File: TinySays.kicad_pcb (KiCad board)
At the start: 2 copper layers, 50 x 50 mm, 30 parts, among them IC1 ATTINY85-S, P2 USB_OTG, P3 CONN_01X02, SW1 Switch_SPDT_x2, U1 MCP73831

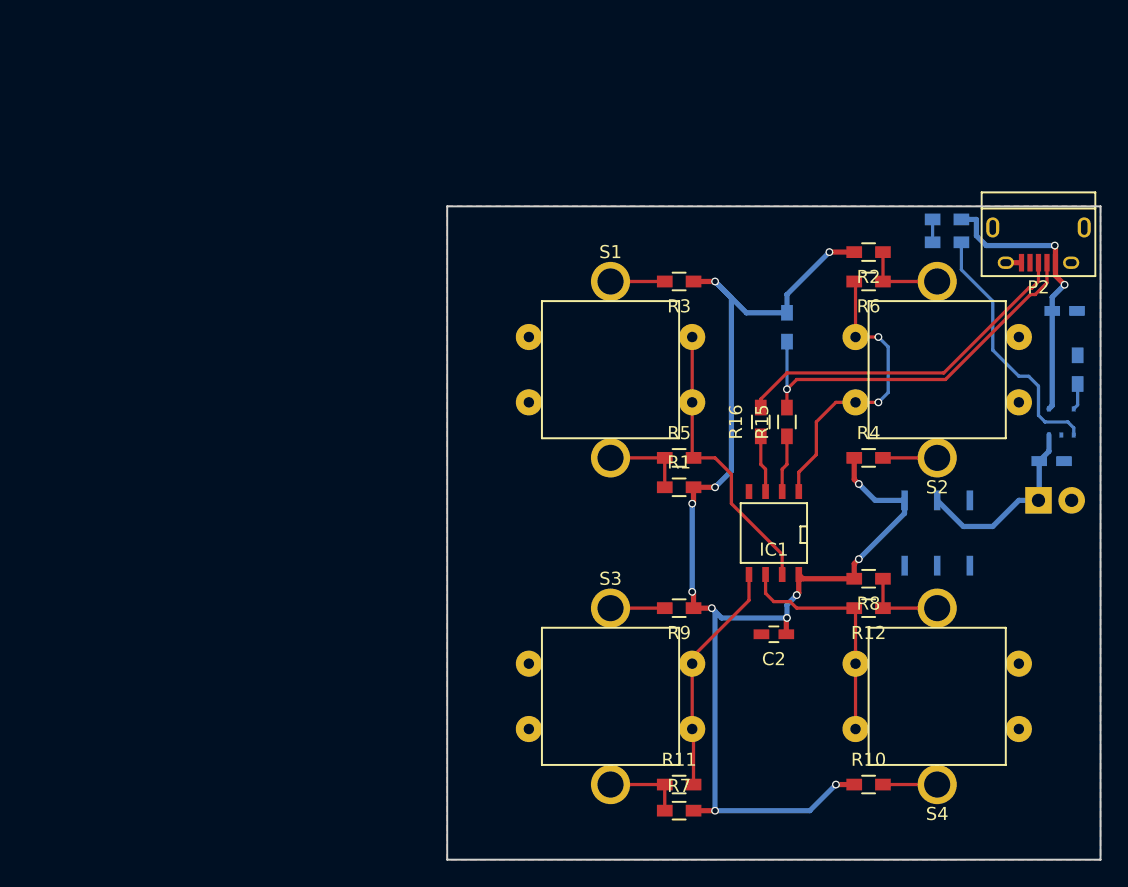
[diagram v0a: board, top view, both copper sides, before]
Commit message: PCB v2.0 40mm x 40mm done
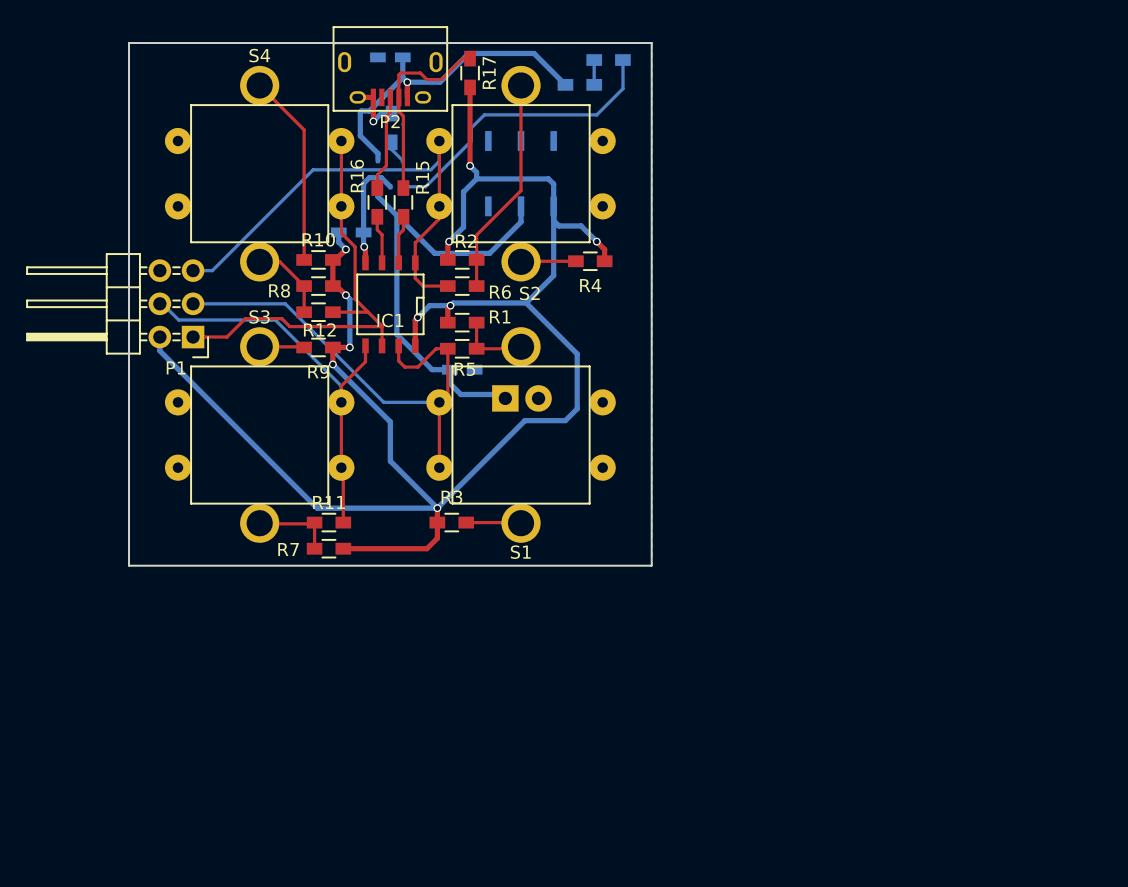
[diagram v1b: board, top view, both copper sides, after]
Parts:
- added P1: CONN_02X03, Pin_Headers:Pin_Header_Angled_2x03, F.Cu at (90.8, 68.0)
- C2: moved to B.Cu
- R17: moved to F.Cu
- moved S4 65.5 mm to (95.9, 55.5), turned to 0 degrees
- moved R10 58.2 mm to (100.4, 62.1), turned to 180 degrees
- moved R14 55.7 mm to (106.0, 52.0)
- moved C1 55.1 mm to (105.9, 46.6), turned to 180 degrees
- moved U1 54.8 mm to (105.9, 55.5)
- moved P2 51.2 mm to (105.9, 48.1)
- moved R12 47.8 mm to (100.4, 66.1), turned to 0 degrees
- moved R8 47.7 mm to (100.4, 64.1), turned to 0 degrees
- moved C3 45.6 mm to (111.4, 70.5)
- moved C2 44.6 mm to (102.9, 60.0), turned to 0 degrees
- moved SW1 42.1 mm to (115.9, 55.5), turned to 0 degrees
- moved P3 41.5 mm to (114.7, 72.7)
- moved S2 35.2 mm to (115.9, 55.5)
- moved IC1 34.2 mm to (105.9, 65.5)
- moved R9 34.1 mm to (100.4, 68.8)
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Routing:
- net VCC: track 103.1 -> 137.3 mm, vias 12 -> 10
- net Net-(C3-Pad1): track 14.8 -> 35.5 mm
- net D+: track 27.1 -> 7.35 mm
- net Net-(IC1-Pad6): track 18.0 -> 35.0 mm
- net Net-(IC1-Pad7): track 22.0 -> 36.9 mm
- net Net-(IC1-Pad1): track 22.9 -> 37.8 mm, vias 2 -> 0
- net D-: track 29.9 -> 15.2 mm, vias 1 -> 0
- net Net-(IC1-Pad5): track 17.9 -> 32.3 mm
- net GND: track 1.27 -> 13.3 mm, vias 0 -> 2
- net Net-(R10-Pad2): track 4.15 -> 14.8 mm
- net Net-(R2-Pad1): track 6.40 -> 16.8 mm
- net Net-(C1-Pad1): track 22.0 -> 25.8 mm, vias 2 -> 1
- net Net-(D1-Pad1): track 19.8 -> 22.7 mm
- net Net-(R1-Pad1): track 6.40 -> 5.46 mm
- net Net-(R9-Pad2): track 4.15 -> 3.42 mm
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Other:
- board size 50 x 50 mm -> 40 x 40 mm

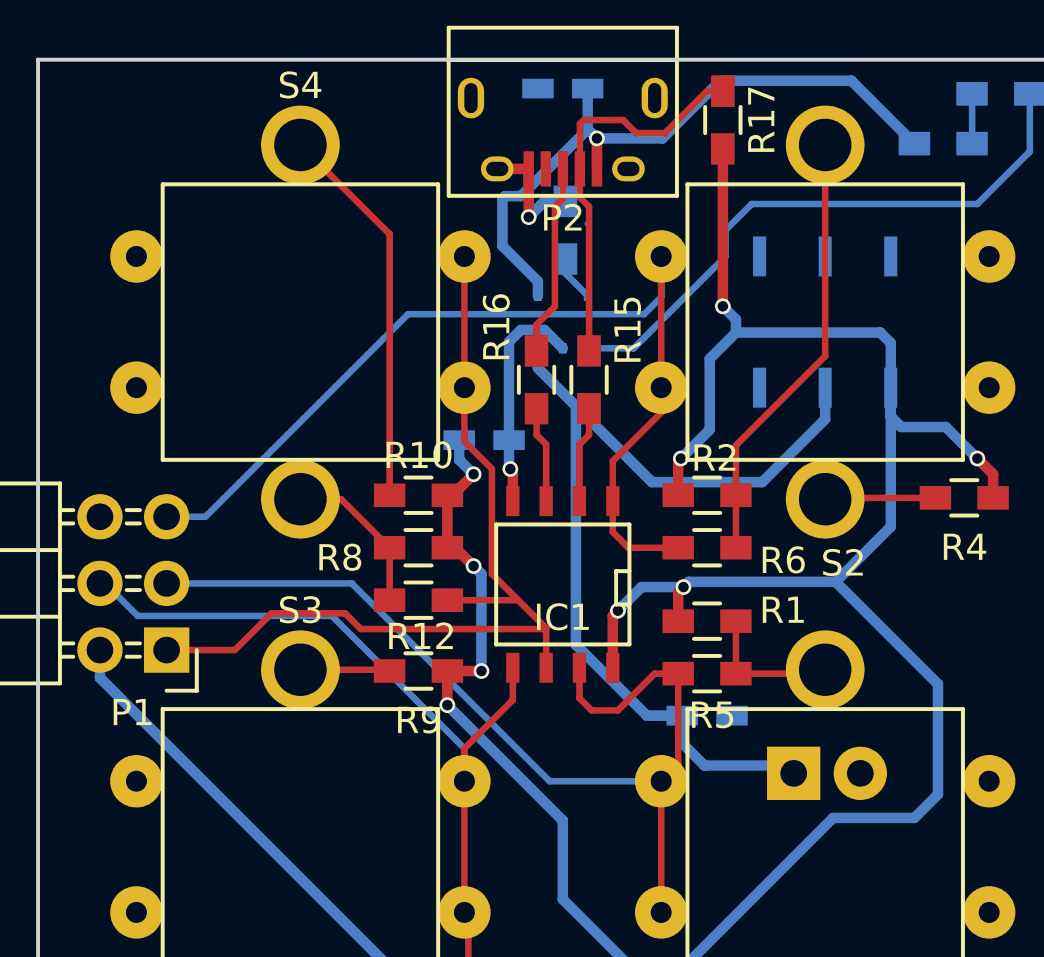
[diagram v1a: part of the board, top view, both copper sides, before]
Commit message: Changed the position of the battery connector.
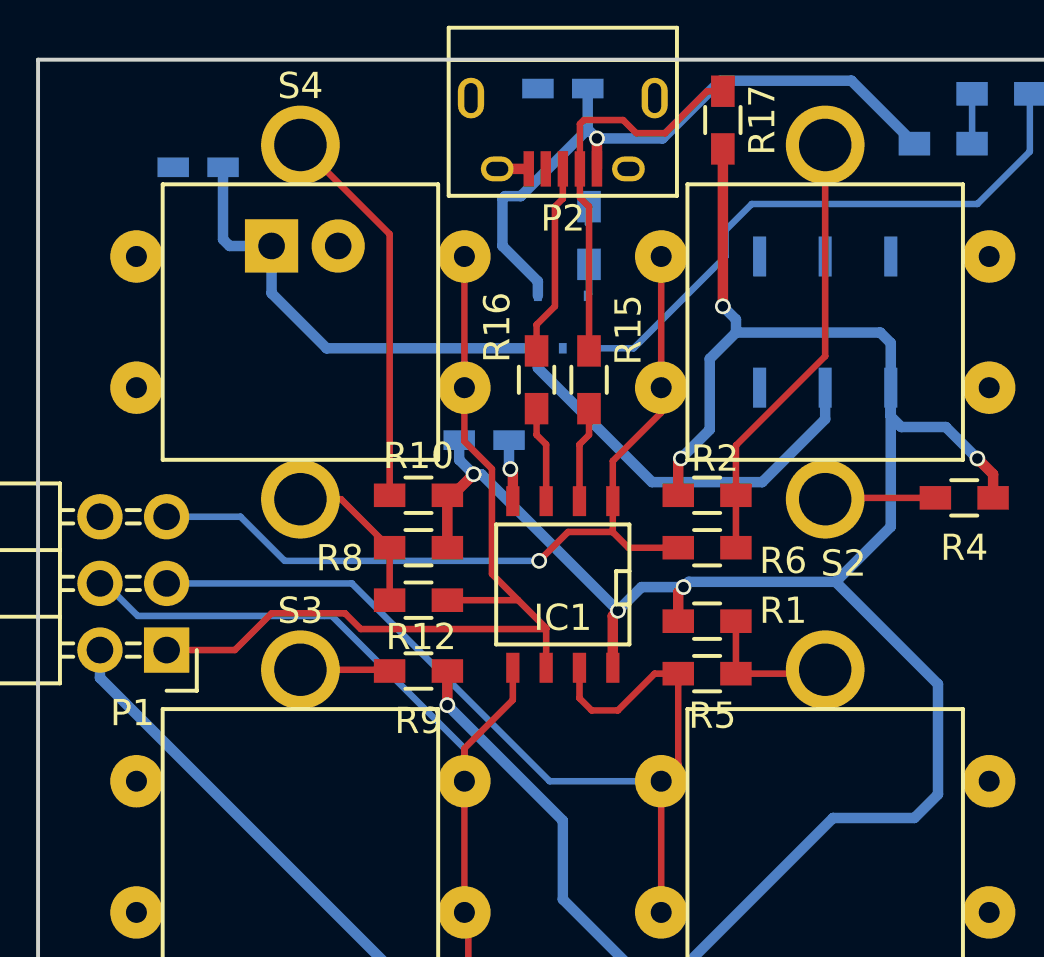
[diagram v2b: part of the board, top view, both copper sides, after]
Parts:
- moved C3 28.5 mm to (92.0, 49.6), turned to 180 degrees
- moved P3 28.3 mm to (94.8, 52.6)
- moved R14 0.92 mm to (106.9, 52.2)
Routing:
- net GND: track 13.3 -> 3.66 mm, vias 2 -> 1
- net Net-(IC1-Pad1): track 37.8 -> 32.2 mm, vias 0 -> 1
- net Net-(C3-Pad1): track 35.5 -> 33.2 mm
- net VCC: track 137.3 -> 138.6 mm, vias 10 -> 8
- net Net-(R14-Pad2): track 1.75 -> 1.22 mm
